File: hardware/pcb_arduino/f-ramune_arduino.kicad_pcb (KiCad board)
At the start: 2 copper layers, 73.7 x 55.9 mm, 15 parts, among them Q1 IRL520N, SW1 SW_Push, U1 74HC595, U2 74HC595, U3 Memory (Socket)

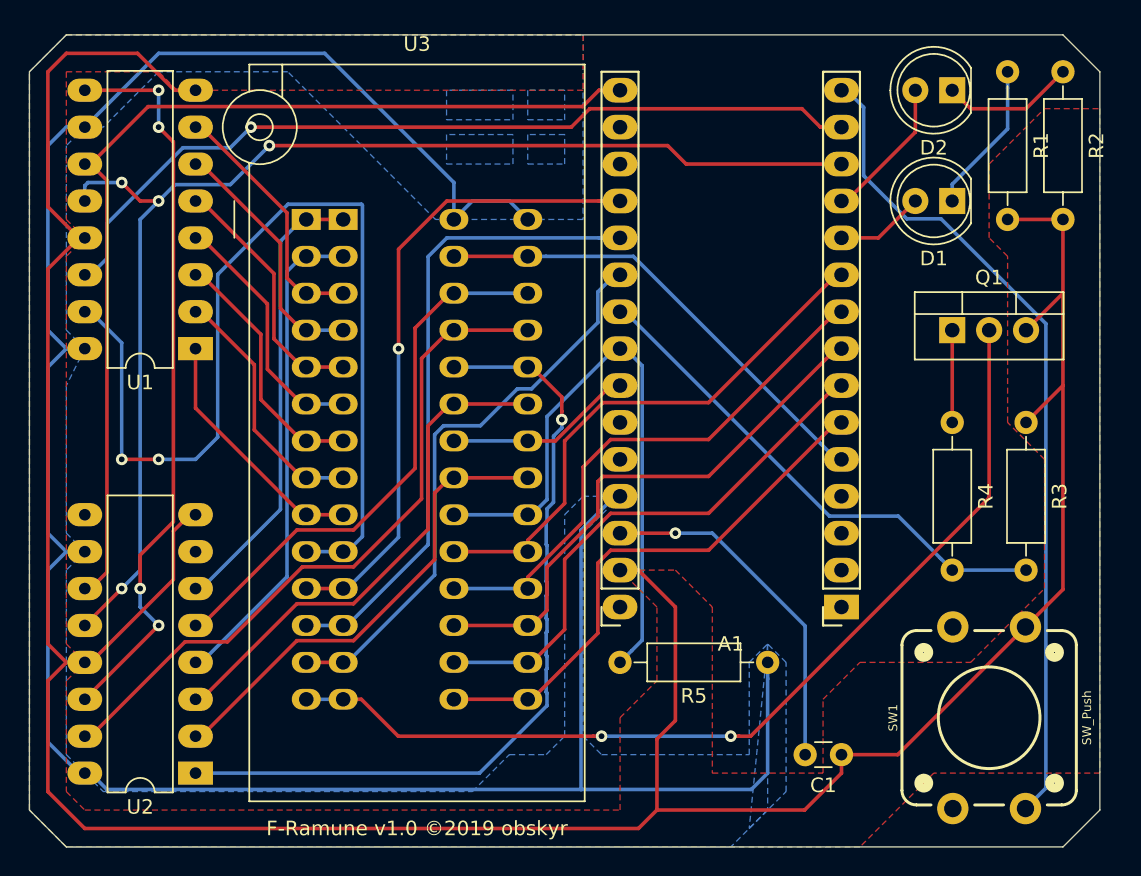
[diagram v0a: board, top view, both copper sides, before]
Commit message: Add more silkscreen indicators onto the board to make it easier to assemble.
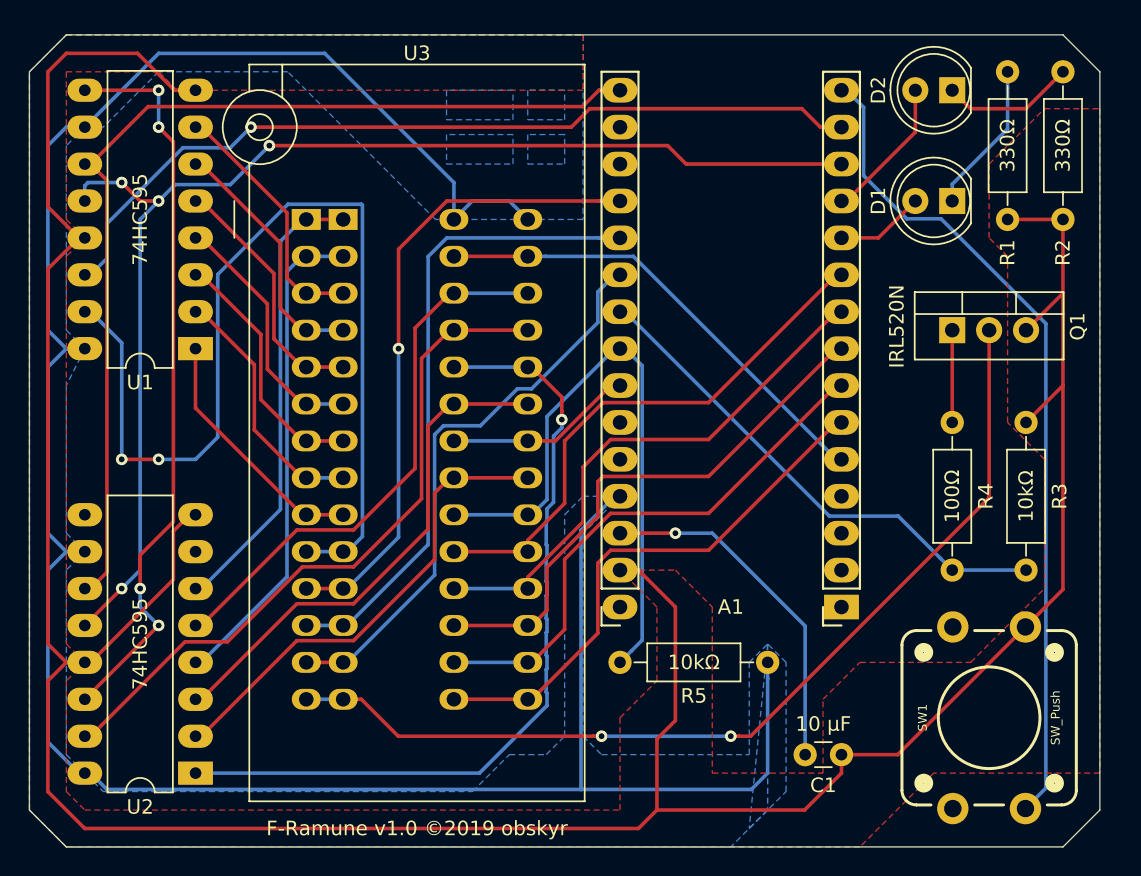
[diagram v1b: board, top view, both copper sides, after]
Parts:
- C1: value 10 µF (optional) -> 10 µF
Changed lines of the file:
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@@
     (solder_mask_min_width 0.25)
     (aux_axis_origin 0 0)
-    (visible_elements FFFFFF7F)
+    (visible_elements 7FFFFFFF)
     (pcbplotparams
-      (layerselection 0x010fc_ffffffff)
-      (usegerberextensions false)
+      (layerselection 0x010f0_ffffffff)
+      (usegerberextensions true)
       (usegerberattributes false)
       (usegerberadvancedattributes false)
@@
       (outputformat 1)
       (mirror false)
-      (drillshape 1)
+      (drillshape 0)
       (scaleselection 1)
-      (outputdirectory ""))
+      (outputdirectory "gerber/"))
   )
   (net 0 "")
@@
       (effects (font (size 1 1) (thickness 0.15)))
     )
-    (fp_text value "10 µF (optional)" (at 1.25 2.11 180) (layer F.Fab)
+    (fp_text value "10 µF" (at 1.25 2.11 180) (layer F.SilkS)
       (effects (font (size 1 1) (thickness 0.15)))
     )
@@
     (descr "28-pin DIP socket with alternative holes for wide ZIF, narrow ZIF, and regular DIP")
     (tags "THT DIP DIL ZIF 7.62mm 10.16mm 15.24mm 300mil 400mil 600mil Socket")
-    (fp_text reference U3 (at 7.62 -12.065) (layer F.SilkS)
+    (fp_text reference U3 (at 7.62 -11.43) (layer F.SilkS)
       (effects (font (size 1 1) (thickness 0.15)))
     )
@@
       (effects (font (size 1 1) (thickness 0.15)))
     )
-    (fp_text value 74HC595 (at 3.81 20.11 180) (layer F.Fab)
+    (fp_text value 74HC595 (at 3.81 8.89 270) (layer F.SilkS)
       (effects (font (size 1 1) (thickness 0.15)))
     )
@@
       (effects (font (size 1 1) (thickness 0.15)))
     )
-    (fp_text value 74HC595 (at 3.81 20.11 180) (layer F.Fab)
+    (fp_text value 74HC595 (at 3.81 8.89 270) (layer F.SilkS)
       (effects (font (size 1 1) (thickness 0.15)))
     )
@@
     (tags "MOMENTARY SWITCH (PUSHBUTTON) - SPST - PTH, 12MM SQUARE")
     (attr virtual)
-    (fp_text reference SW1 (at 0 -6.604 90) (layer F.SilkS)
+    (fp_text reference SW1 (at 0 -4.572 90) (layer F.SilkS)
       (effects (font (size 0.6096 0.6096) (thickness 0.127)))
     )
-    (fp_text value SW_Push (at 0 6.731 90) (layer F.SilkS)
+    (fp_text value SW_Push (at 0 4.572 90) (layer F.SilkS)
       (effects (font (size 0.6096 0.6096) (thickness 0.127)))
     )
@@
       (effects (font (size 1 1) (thickness 0.15)))
     )
-    (fp_text value 10kΩ (at 5.08 2.31 180) (layer F.Fab)
+    (fp_text value 10kΩ (at 5.08 0 180) (layer F.SilkS)
       (effects (font (size 1 1) (thickness 0.15)))
     )
@@
       (effects (font (size 1 1) (thickness 0.15)))
     )
-    (fp_text value 100Ω (at 5.08 2.31 270) (layer F.Fab)
+    (fp_text value 100Ω (at 5.08 0 270) (layer F.SilkS)
       (effects (font (size 1 1) (thickness 0.15)))
     )
@@
       (effects (font (size 1 1) (thickness 0.15)))
     )
-    (fp_text value 10kΩ (at 5.08 2.31 270) (layer F.Fab)
+    (fp_text value 10kΩ (at 5.08 0 270) (layer F.SilkS)
       (effects (font (size 1 1) (thickness 0.15)))
     )
@@
     (descr "Resistor, Axial_DIN0207 series, Axial, Horizontal, pin pitch=10.16mm, 0.25W = 1/4W, length*diameter=6.3*2.5mm^2, http://cdn-reichelt.de/documents/datenblatt/B400/1_4W%23YAG.pdf")
     (tags "Resistor Axial_DIN0207 series Axial Horizontal pin pitch 10.16mm 0.25W = 1/4W length 6.3mm diameter 2.5mm")
-    (fp_text reference R2 (at 5.08 -2.31 270) (layer F.SilkS)
-      (effects (font (size 1 1) (thickness 0.15)))
-    )
-    (fp_text value 330Ω (at 5.08 2.31 270) (layer F.Fab)
+    (fp_text reference R2 (at 12.446 0 90) (layer F.SilkS)
+      (effects (font (size 1 1) (thickness 0.15)))
+    )
+    (fp_text value 330Ω (at 5.08 0 270) (layer F.SilkS)
       (effects (font (size 1 1) (thickness 0.15)))
     )
@@
     (descr "Resistor, Axial_DIN0207 series, Axial, Horizontal, pin pitch=10.16mm, 0.25W = 1/4W, length*diameter=6.3*2.5mm^2, http://cdn-reichelt.de/documents/datenblatt/B400/1_4W%23YAG.pdf")
     (tags "Resistor Axial_DIN0207 series Axial Horizontal pin pitch 10.16mm 0.25W = 1/4W length 6.3mm diameter 2.5mm")
-    (fp_text reference R1 (at 5.08 -2.31 270) (layer F.SilkS)
-      (effects (font (size 1 1) (thickness 0.15)))
-    )
-    (fp_text value 330Ω (at 5.08 2.31 270) (layer F.Fab)
+    (fp_text reference R1 (at 12.446 0 90) (layer F.SilkS)
+      (effects (font (size 1 1) (thickness 0.15)))
+    )
+    (fp_text value 330Ω (at 5.08 0 270) (layer F.SilkS)
       (effects (font (size 1 1) (thickness 0.15)))
     )
@@
     (descr "TO-220-3, Vertical, RM 2.54mm")
     (tags "TO-220-3 Vertical RM 2.54mm")
-    (fp_text reference Q1 (at 2.54 -3.62) (layer F.SilkS)
-      (effects (font (size 1 1) (thickness 0.15)))
-    )
-    (fp_text value IRL520N (at 2.54 3.92) (layer F.Fab)
+    (fp_text reference Q1 (at 8.636 -0.254 90) (layer F.SilkS)
+      (effects (font (size 1 1) (thickness 0.15)))
+    )
+    (fp_text value IRL520N (at -3.81 -0.254 90) (layer F.SilkS)
       (effects (font (size 1 1) (thickness 0.15)))
     )
@@
     (descr "LED, diameter 5.0mm, 2 pins, http://cdn-reichelt.de/documents/datenblatt/A500/LL-504BC2E-009.pdf")
     (tags "LED diameter 5.0mm 2 pins")
-    (fp_text reference D2 (at 1.27 -3.96 180) (layer F.SilkS)
+    (fp_text reference D2 (at 5.08 0 270) (layer F.SilkS)
       (effects (font (size 1 1) (thickness 0.15)))
     )
@@
     (descr "LED, diameter 5.0mm, 2 pins, http://cdn-reichelt.de/documents/datenblatt/A500/LL-504BC2E-009.pdf")
     (tags "LED diameter 5.0mm 2 pins")
-    (fp_text reference D1 (at 1.27 -3.96 180) (layer F.SilkS)
+    (fp_text reference D1 (at 5.08 0 270) (layer F.SilkS)
       (effects (font (size 1 1) (thickness 0.15)))
     )
@@
     (descr "Through hole straight socket strips to fit an Arduino Nano, 1x15, 2.54mm pitch")
     (tags "Through hole socket strip THT 2x15 2.54mm double row Arduino Nano")
-    (fp_text reference A1 (at 0 -2.54 180) (layer F.SilkS)
+    (fp_text reference A1 (at 0 0 180) (layer F.SilkS)
       (effects (font (size 1 1) (thickness 0.15)))
     )
@@
       (effects (font (size 1 1) (thickness 0.15)))
     )
-    (fp_text user %R (at 0 -2.54 180) (layer F.Fab)
+    (fp_text user %R (at 0 0 180) (layer F.Fab)
       (effects (font (size 1 1) (thickness 0.15)))
     )
@@
   (segment (start 154.12641 81.28) (end 132.08 81.28) (width 0.25) (layer F.Cu) (net 4))
   (segment (start 132.08 81.28) (end 132.08 81.28) (width 0.25) (layer F.Cu) (net 4))
-  (via (at 132.08 81.28) (size 0.8) (drill 0.4) (layers F.Cu B.Cu) (net 4))
+  (via (at 132.08 81.28) (size 0.8) (drill 0.4) (layers F.Cu B.Cu) (net 4) (status 1000000))
   (segment (start 121.05 91.44) (end 120.65 91.44) (width 0.25) (layer B.Cu) (net 4))
   (segment (start 122.17501 90.31499) (end 121.05 91.44) (width 0.25) (layer B.Cu) (net 4))

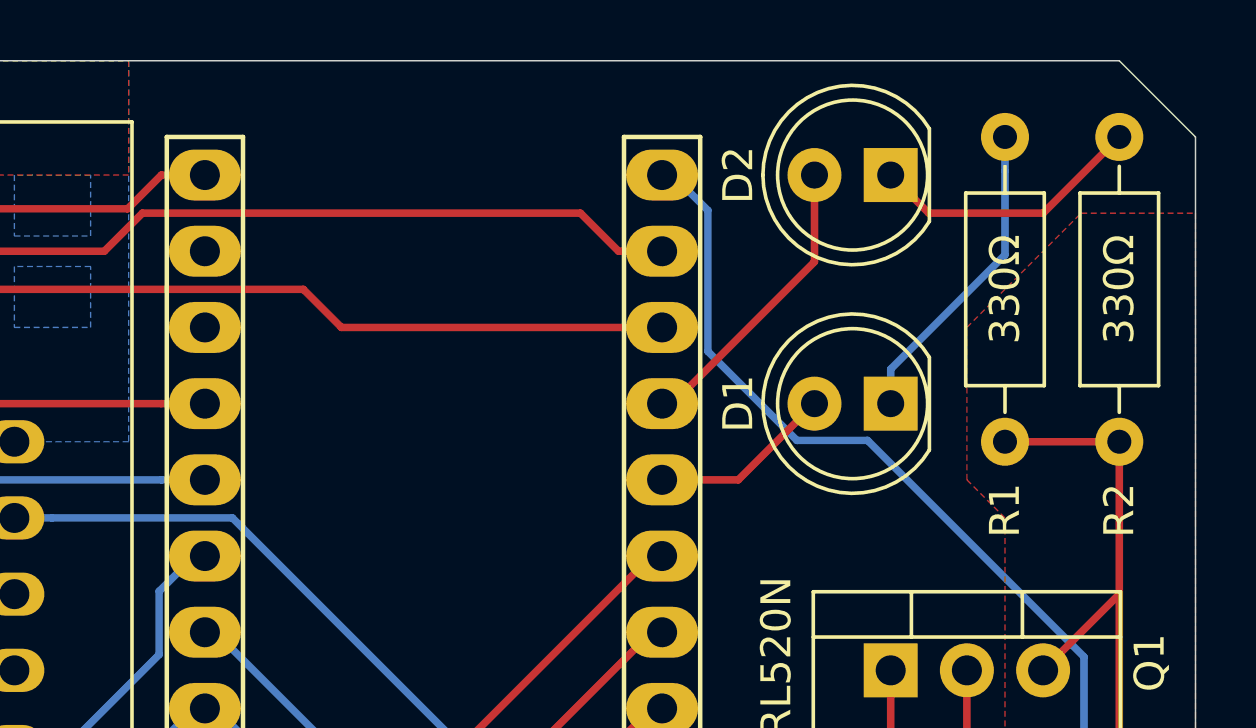
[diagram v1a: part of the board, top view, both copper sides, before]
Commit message: Last-minute silkscreen changes to indicate LED colors and Arduino orientation. Also, delete the redundant NPTH file as this design only has plated holes.
It's called last-minute, because the cutoff for changes to my PCB order is 2 hours from now and I just noticed the design issue.
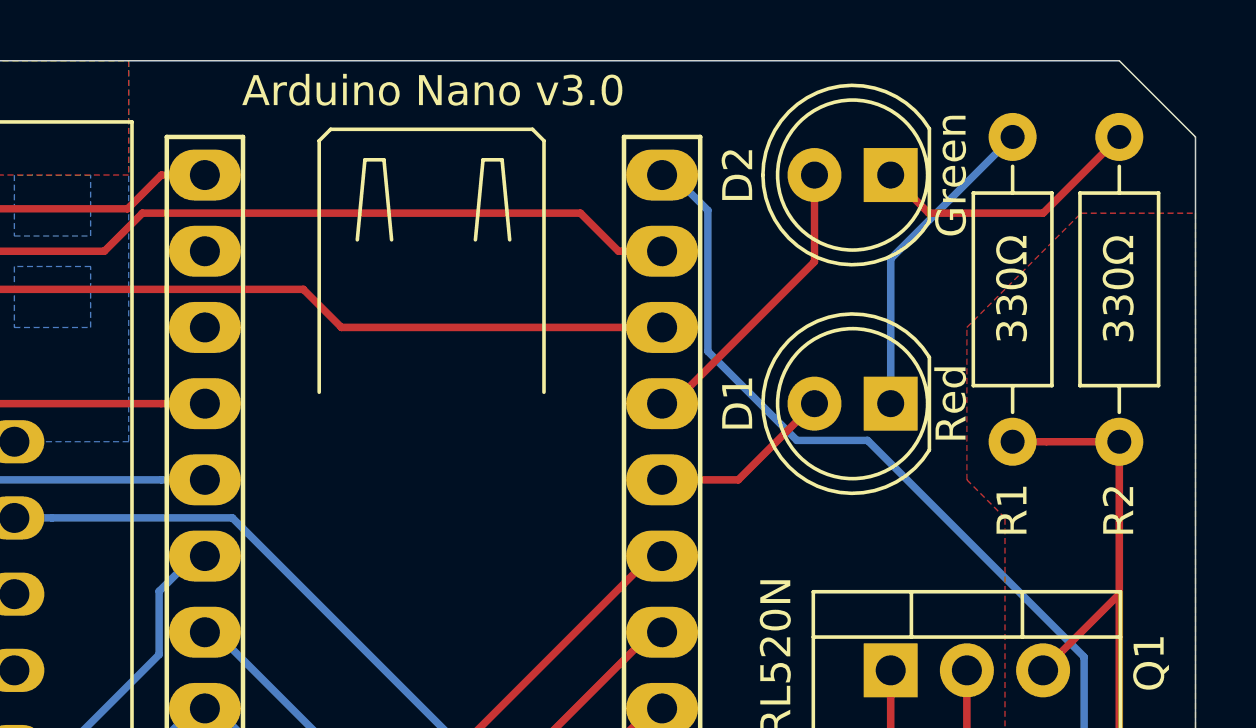
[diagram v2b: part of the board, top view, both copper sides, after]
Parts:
- A1: value Arduino_Nano_v3.x -> Arduino Nano v3.0
- D1: value LED_Red -> Red
- D2: value LED_Green -> Green
- moved R1 0.25 mm to (184.4, 77.5)
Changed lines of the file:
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@@
   (general
     (thickness 1.6)
-    (drawings 16)
-    (tracks 408)
+    (drawings 27)
+    (tracks 407)
     (zones 0)
     (modules 15)
@@
   )
   (module f-ramune:R_Axial_DIN0207_L6.3mm_D2.5mm_P10.16mm_Horizontal (layer F.Cu)
-    (at 184.15 77.47 270)
+    (at 184.404 77.47 270)
     (descr "Resistor, Axial_DIN0207 series, Axial, Horizontal, pin pitch=10.16mm, 0.25W = 1/4W, length*diameter=6.3*2.5mm^2, http://cdn-reichelt.de/documents/datenblatt/B400/1_4W%23YAG.pdf")
     (tags "Resistor Axial_DIN0207 series Axial Horizontal pin pitch 10.16mm 0.25W = 1/4W length 6.3mm diameter 2.5mm")
@@
       (effects (font (size 1 1) (thickness 0.15)))
     )
-    (fp_text value LED_Green (at 1.27 3.96 180) (layer F.Fab)
+    (fp_text value Green (at -2.032 0 270) (layer F.SilkS)
       (effects (font (size 1 1) (thickness 0.15)))
     )
@@
       (effects (font (size 1 1) (thickness 0.15)))
     )
-    (fp_text value LED_Red (at 1.27 3.96 180) (layer F.Fab)
+    (fp_text value Red (at -2.032 0 270) (layer F.SilkS)
       (effects (font (size 1 1) (thickness 0.15)))
     )
@@
       (effects (font (size 1 1) (thickness 0.15)))
     )
-    (fp_text value Arduino_Nano_v3.x (at 0 38.1 180) (layer F.Fab)
+    (fp_text value "Arduino Nano v3.0" (at 0 38.354 180) (layer F.SilkS)
       (effects (font (size 1 1) (thickness 0.15)))
     )
@@
     )
   )
+  (gr_line (start 166.497 80.899) (end 166.751 78.232) (layer F.SilkS) (width 0.12))
+  (gr_line (start 166.751 78.232) (end 167.386 78.232) (layer F.SilkS) (width 0.12))
+  (gr_line (start 167.386 78.232) (end 167.64 80.899) (layer F.SilkS) (width 0.12))
+  (gr_line (start 163.449 78.232) (end 163.703 80.899) (layer F.SilkS) (width 0.12))
+  (gr_line (start 162.814 78.232) (end 163.449 78.232) (layer F.SilkS) (width 0.12))
+  (gr_line (start 162.56 80.899) (end 162.814 78.232) (layer F.SilkS) (width 0.12))
+  (gr_line (start 168.783 77.597) (end 168.783 85.979) (layer F.SilkS) (width 0.12))
+  (gr_line (start 168.402 77.216) (end 168.783 77.597) (layer F.SilkS) (width 0.12))
+  (gr_line (start 161.671 77.216) (end 168.402 77.216) (layer F.SilkS) (width 0.12))
+  (gr_line (start 161.29 77.597) (end 161.671 77.216) (layer F.SilkS) (width 0.12))
+  (gr_line (start 161.29 85.979) (end 161.29 77.597) (layer F.SilkS) (width 0.12))
   (gr_poly (pts (xy 145.542 80.772) (xy 150.114 80.772) (xy 150.114 78.74) (xy 151.13 78.74) (xy 151.13 80.772) (xy 153.67 80.772) (xy 153.67 81.788) (xy 151.13 81.788) (xy 151.13 83.82) (xy 150.114 83.82) (xy 150.114 81.788) (xy 145.542 81.788)) (layer B.Mask) (width 0.1))
   (gr_line (start 145.542 83.82) (end 145.542 78.74) (layer B.SilkS) (width 0.12))
@@
   (segment (start 154.12641 81.28) (end 132.08 81.28) (width 0.25) (layer F.Cu) (net 4))
   (segment (start 132.08 81.28) (end 132.08 81.28) (width 0.25) (layer F.Cu) (net 4))
-  (via (at 132.08 81.28) (size 0.8) (drill 0.4) (layers F.Cu B.Cu) (net 4) (status 1000000))
+  (via (at 132.08 81.28) (size 0.8) (drill 0.4) (layers F.Cu B.Cu) (net 4))
   (segment (start 121.05 91.44) (end 120.65 91.44) (width 0.25) (layer B.Cu) (net 4))
   (segment (start 122.17501 90.31499) (end 121.05 91.44) (width 0.25) (layer B.Cu) (net 4))
@@
   (segment (start 130.66501 82.69499) (end 127.404006 82.69499) (width 0.25) (layer B.Cu) (net 4))
   (segment (start 132.08 81.28) (end 130.66501 82.69499) (width 0.25) (layer B.Cu) (net 4))
-  (segment (start 184.15 87.63) (end 187.96 87.63) (width 0.25) (layer F.Cu) (net 5))
   (segment (start 187.96 92.71) (end 185.42 95.25) (width 0.25) (layer F.Cu) (net 5))
   (segment (start 187.96 87.63) (end 187.96 92.71) (width 0.25) (layer F.Cu) (net 5))
@@
   (segment (start 157.48 111.76) (end 158.75 111.76) (width 0.25) (layer F.Cu) (net 5))
   (segment (start 158.75 111.76) (end 161.29 114.3) (width 0.25) (layer F.Cu) (net 5))
+  (segment (start 185.53537 87.63) (end 187.96 87.63) (width 0.25) (layer F.Cu) (net 5))
+  (segment (start 184.404 87.63) (end 185.53537 87.63) (width 0.25) (layer F.Cu) (net 5))
   (segment (start 162.031715 83.82) (end 160.761715 82.55) (width 0.25) (layer F.Cu) (net 6))
   (segment (start 172.72 83.82) (end 162.031715 83.82) (width 0.25) (layer F.Cu) (net 6))
@@
   (via (at 165.099972 123.19) (size 0.8) (drill 0.4) (layers F.Cu B.Cu) (net 49))
   (segment (start 166.465002 123.19) (end 165.665657 123.19) (width 0.25) (layer F.Cu) (net 49))
-  (segment (start 184.15 78.60137) (end 184.15 77.47) (width 0.25) (layer B.Cu) (net 50))
-  (segment (start 184.15 81.4) (end 184.15 78.60137) (width 0.25) (layer B.Cu) (net 50))
-  (segment (start 180.34 85.21) (end 184.15 81.4) (width 0.25) (layer B.Cu) (net 50))
-  (segment (start 180.34 86.36) (end 180.34 85.21) (width 0.25) (layer B.Cu) (net 50))
+  (segment (start 180.34 81.534) (end 184.404 77.47) (width 0.25) (layer B.Cu) (net 50))
+  (segment (start 180.34 86.36) (end 180.34 81.534) (width 0.25) (layer B.Cu) (net 50))
   (segment (start 185.42 80.01) (end 187.96 77.47) (width 0.25) (layer F.Cu) (net 51))
   (segment (start 180.34 78.74) (end 181.61 80.01) (width 0.25) (layer F.Cu) (net 51))
